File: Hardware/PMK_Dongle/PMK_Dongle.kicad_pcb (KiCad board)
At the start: 4 copper layers, 10.4 x 18.3 mm, 32 parts, among them IC1 ESP32-S2FH4, J1 USB_A, U1 MIC5528-3.3YMT-T5, Y1 Crystal_GND24_Small

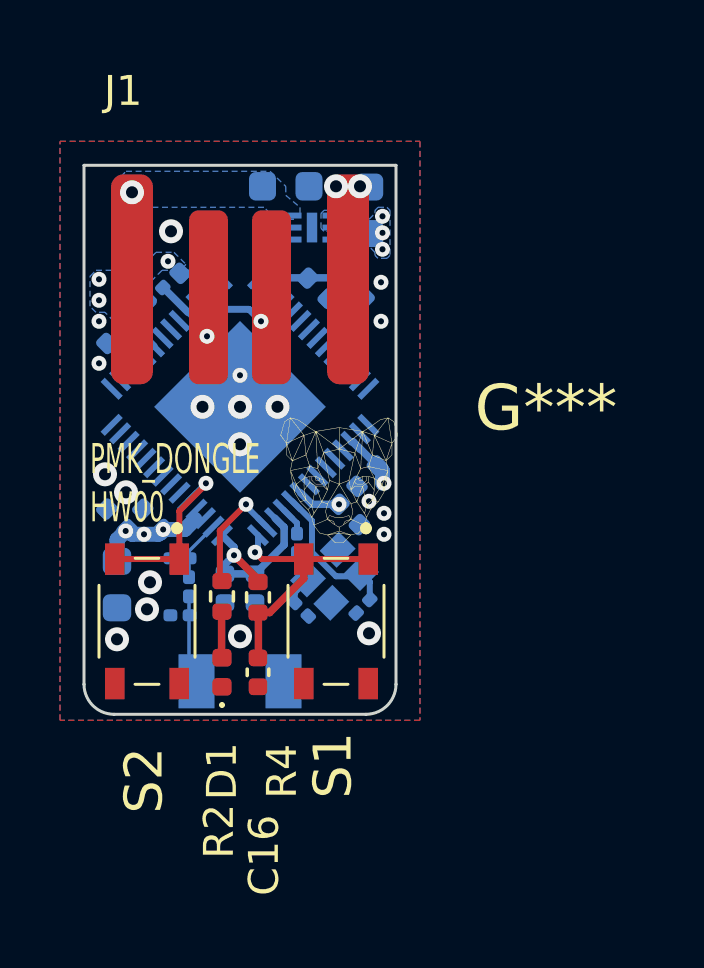
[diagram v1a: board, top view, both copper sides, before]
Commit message: HW00 of keyboard is done but ugly
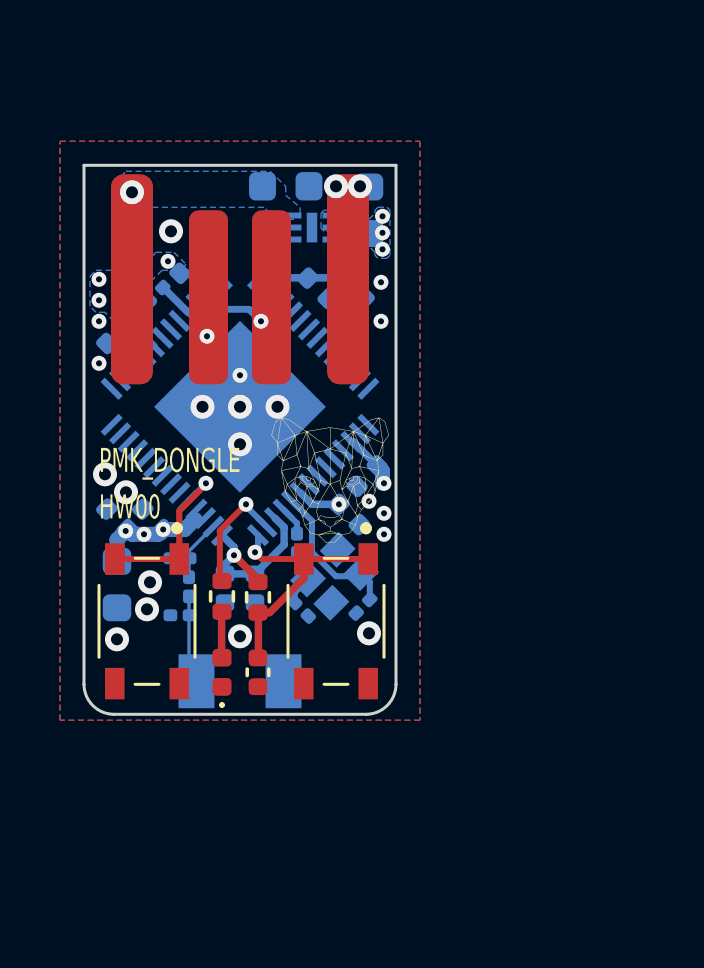
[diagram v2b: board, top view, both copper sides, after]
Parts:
- moved G*** 0.30 mm to (156.0, 43.7)
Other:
- board text added: "HW00"
- board text added: "PMK_DONGLE"
- board text removed: "PMK_DONGLE HW00"
